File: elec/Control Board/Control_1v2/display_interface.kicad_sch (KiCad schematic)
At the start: 20 parts, among them J35 Conn_02x05_Odd_Even, J36 Conn_02x05_Odd_Even, J801 Conn_01x03_0.1", J802 Con_01x02_0.1", J803 Screw_Terminal_01x04_5.08mm, J804 Screw_Terminal_01x02_5.08mm, J805 Con_01x02_0.1", K801 Relay SRU-12VDC, Q601 BSS138

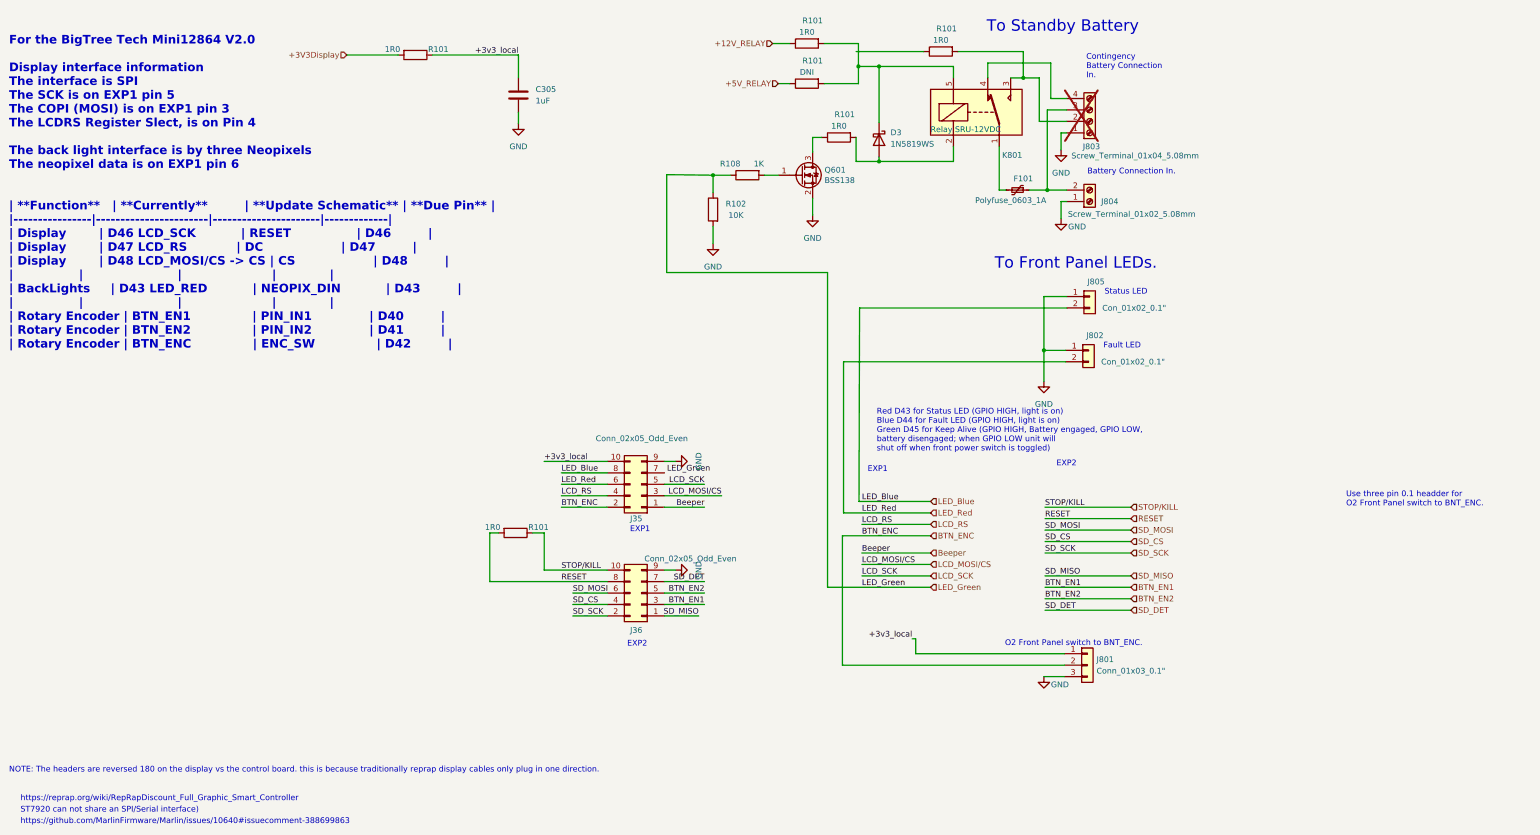
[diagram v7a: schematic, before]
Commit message: Clearing more ERC schematic errors. Off grid. Remove some redundant Net names.
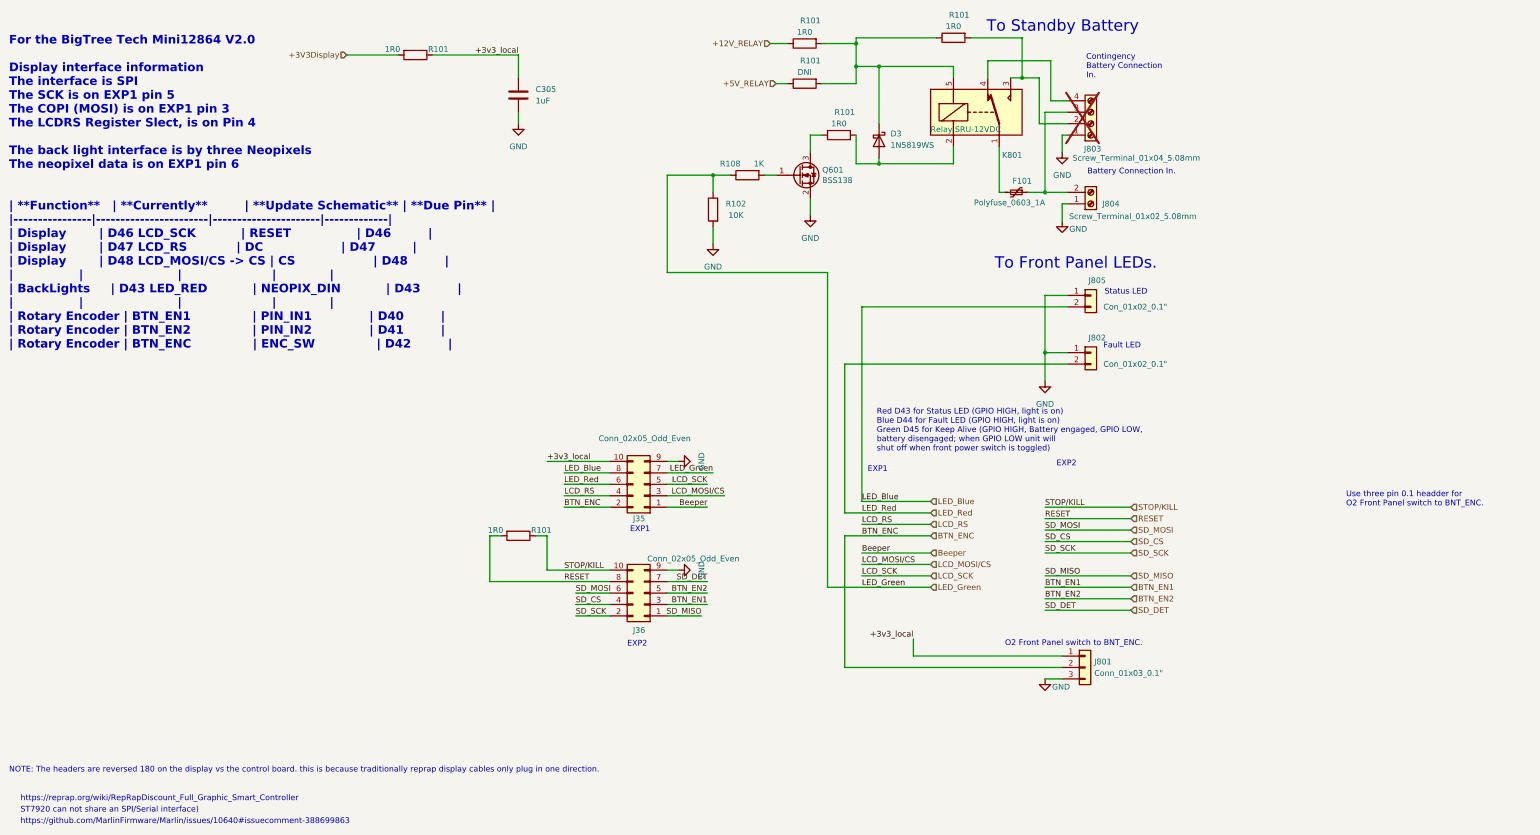
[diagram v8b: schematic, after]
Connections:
- net LED_Green: now also J35.7 (Pin_7)
- net at D3.1 (K), K801.5, R101.2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: now also R101.1
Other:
- moved on the sheet: F101, J35, J36, J801, J802, J803, J804, Q601, R101
